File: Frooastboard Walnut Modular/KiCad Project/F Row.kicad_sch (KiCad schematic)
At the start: 82 parts, among them J12 Conn_01x06_Male, J13 Conn_01x16_Male, J14 Conn_01x10_Male, J18 Conn_01x04_Male

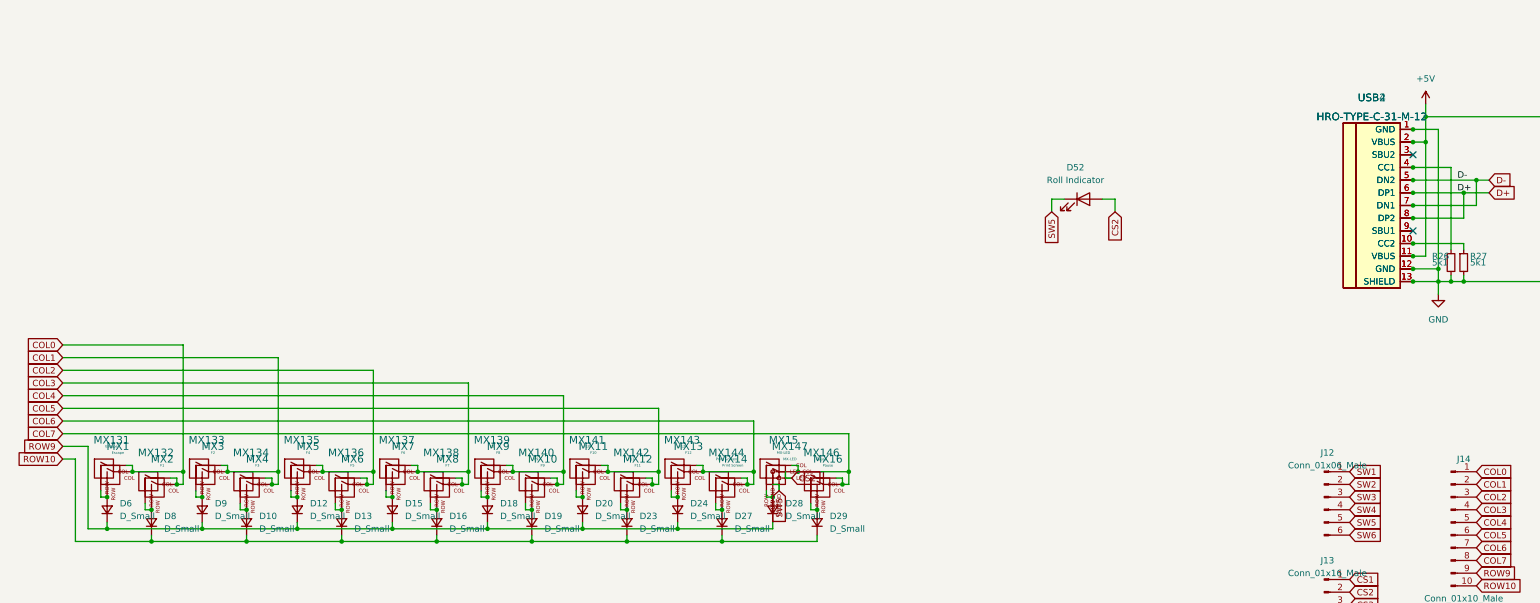
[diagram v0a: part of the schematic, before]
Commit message: actually place leds good
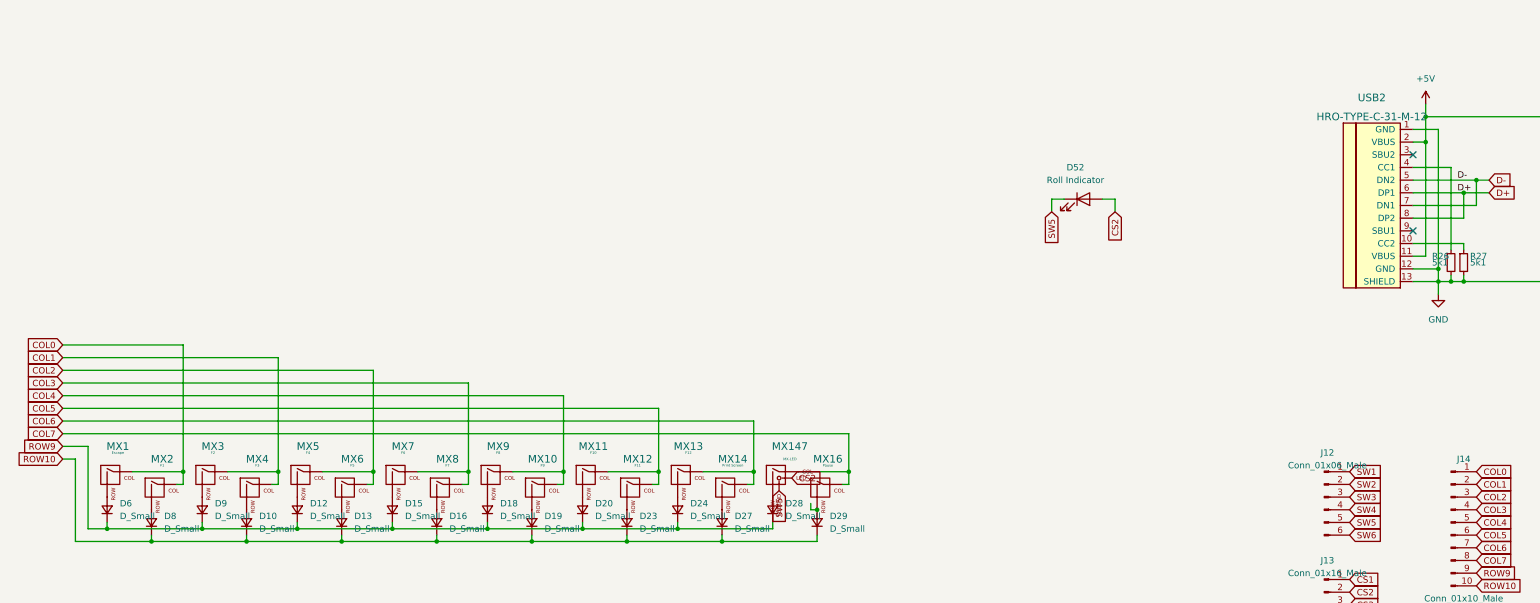
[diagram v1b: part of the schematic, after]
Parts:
- removed MX131: Escape, MX_Only:MXOnly-1U-NoLED, symbol MX_Alps_Hybrid:MX-NoLED
- removed MX132: F1, MX_Only:MXOnly-1U-NoLED, symbol MX_Alps_Hybrid:MX-NoLED
- removed MX133: F2, MX_Only:MXOnly-1U-NoLED, symbol MX_Alps_Hybrid:MX-NoLED
- removed MX134: F3, MX_Only:MXOnly-1U-NoLED, symbol MX_Alps_Hybrid:MX-NoLED
- removed MX135: F4, MX_Only:MXOnly-1U-NoLED, symbol MX_Alps_Hybrid:MX-NoLED
- removed MX136: F5, MX_Only:MXOnly-1U-NoLED, symbol MX_Alps_Hybrid:MX-NoLED
- removed MX137: F6, MX_Only:MXOnly-1U-NoLED, symbol MX_Alps_Hybrid:MX-NoLED
- removed MX138: F7, MX_Only:MXOnly-1U-NoLED, symbol MX_Alps_Hybrid:MX-NoLED
- removed MX139: F8, MX_Only:MXOnly-1U-NoLED, symbol MX_Alps_Hybrid:MX-NoLED
- removed MX140: F9, MX_Only:MXOnly-1U-NoLED, symbol MX_Alps_Hybrid:MX-NoLED
- removed MX141: F10, MX_Only:MXOnly-1U-NoLED, symbol MX_Alps_Hybrid:MX-NoLED
- removed MX142: F11, MX_Only:MXOnly-1U-NoLED, symbol MX_Alps_Hybrid:MX-NoLED
- removed MX143: F12, MX_Only:MXOnly-1U-NoLED, symbol MX_Alps_Hybrid:MX-NoLED
- removed MX144: Print Screen, MX_Only:MXOnly-1U-NoLED, symbol MX_Alps_Hybrid:MX-NoLED
- removed MX146: Pause, MX_Only:MXOnly-1U-NoLED, symbol MX_Alps_Hybrid:MX-NoLED
- removed MX15: MX-LED, MX_Only:MXOnly-1U, symbol MX_Alps_Hybrid:MX-LED
- removed USB4: HRO-TYPE-C-31-M-12, Type_C:HRO-TYPE-C-31-M-12, symbol Type-C:HRO-TYPE-C-31-M-12

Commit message: almost finished bus stuff connector fpc
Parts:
- removed J12: Conn_01x06_Male, Connector_PinHeader_1.27mm:PinHeader_1x06_P1.27mm_Vertical, symbol Connector:Conn_01x06_Pin
- removed J13: Conn_01x16_Male, Connector_PinHeader_1.27mm:PinHeader_1x16_P1.27mm_Vertical, symbol Connector:Conn_01x16_Pin
- removed J14: Conn_01x10_Male, Connector_PinHeader_1.27mm:PinHeader_1x10_P1.27mm_Vertical, symbol Connector:Conn_01x10_Pin
- removed J18: Conn_01x04_Male, Connector_PinHeader_1.27mm:PinHeader_1x04_P1.27mm_Vertical, symbol Connector:Conn_01x04_Pin
- renumbered D93 to D29A, D38 to D29B
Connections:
- net CS2: no longer D52.2 (A)
- net SW5: no longer D11.3 (R-), D14.3 (R-), D17.3 (R-), D21.3 (R-), D25.3 (R-), D29A.3 (R-), D29B.3 (R-), D30.3 (R-), D32.3 (R-), D34.3 (R-), D36.3 (R-), D4.3 (R-), D52.1 (K), D7.3 (R-)
- net COL0 renamed fr_col0
- net COL1 renamed fr_col1
- net COL2 renamed fr_col2
- net COL3 renamed fr_col3
- net COL4 renamed fr_col4
- net COL5 renamed fr_col5
- net COL6 renamed fr_col6
- net COL7 renamed fr_col7
- net CS1 renamed fr_cs1
- net CS10 renamed fr_cs10
- net CS11 renamed fr_cs11
- net CS12 renamed fr_cs12
- net CS13 renamed fr_cs13
- net CS14 renamed fr_cs14
- net CS15 renamed fr_cs15
- net CS16 renamed fr_cs16
- net CS3 renamed fr_cs3
- net CS4 renamed fr_cs4
- net CS5 renamed fr_cs5
- net CS6 renamed fr_cs6
- net CS7 renamed fr_cs7
- net CS8 renamed fr_cs8
- net CS9 renamed fr_cs9
- net D+ renamed fr_dp
- net D- renamed fr_dn
- net ROW10 renamed fr_row11
- net ROW9 renamed fr_row10
- net SW1 renamed fr_sw1
- net SW2 renamed fr_sw2
- net SW3 renamed fr_sw3
- net SW4 renamed fr_sw4
- net SW6 renamed fr_sw6
- new net fr_cs2: D52.2 (A)
- new net fr_sw5: D11.3 (R-), D14.3 (R-), D17.3 (R-), D21.3 (R-), D25.3 (R-), D29A.3 (R-), D29B.3 (R-), D30.3 (R-), D32.3 (R-), D34.3 (R-), D36.3 (R-), D4.3 (R-), D52.1 (K), D7.3 (R-)
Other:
- moved on the sheet: D11, D14, D17, D21, D22, D25, D26, D29A, D29B, D30, D31, D32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
